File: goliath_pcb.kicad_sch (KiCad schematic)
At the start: 34 parts, among them IC1 MCT9001SD, IC2 MCT9001SD, IC3 MCT9001SD, IC4 MCT9001SD, IC5 MCT9001SD, IC6 LTC1298CS8-PBF, J1 RJ45_LED, J2 RJ45_LED, U1 Pico, U2 LM7805_TO220

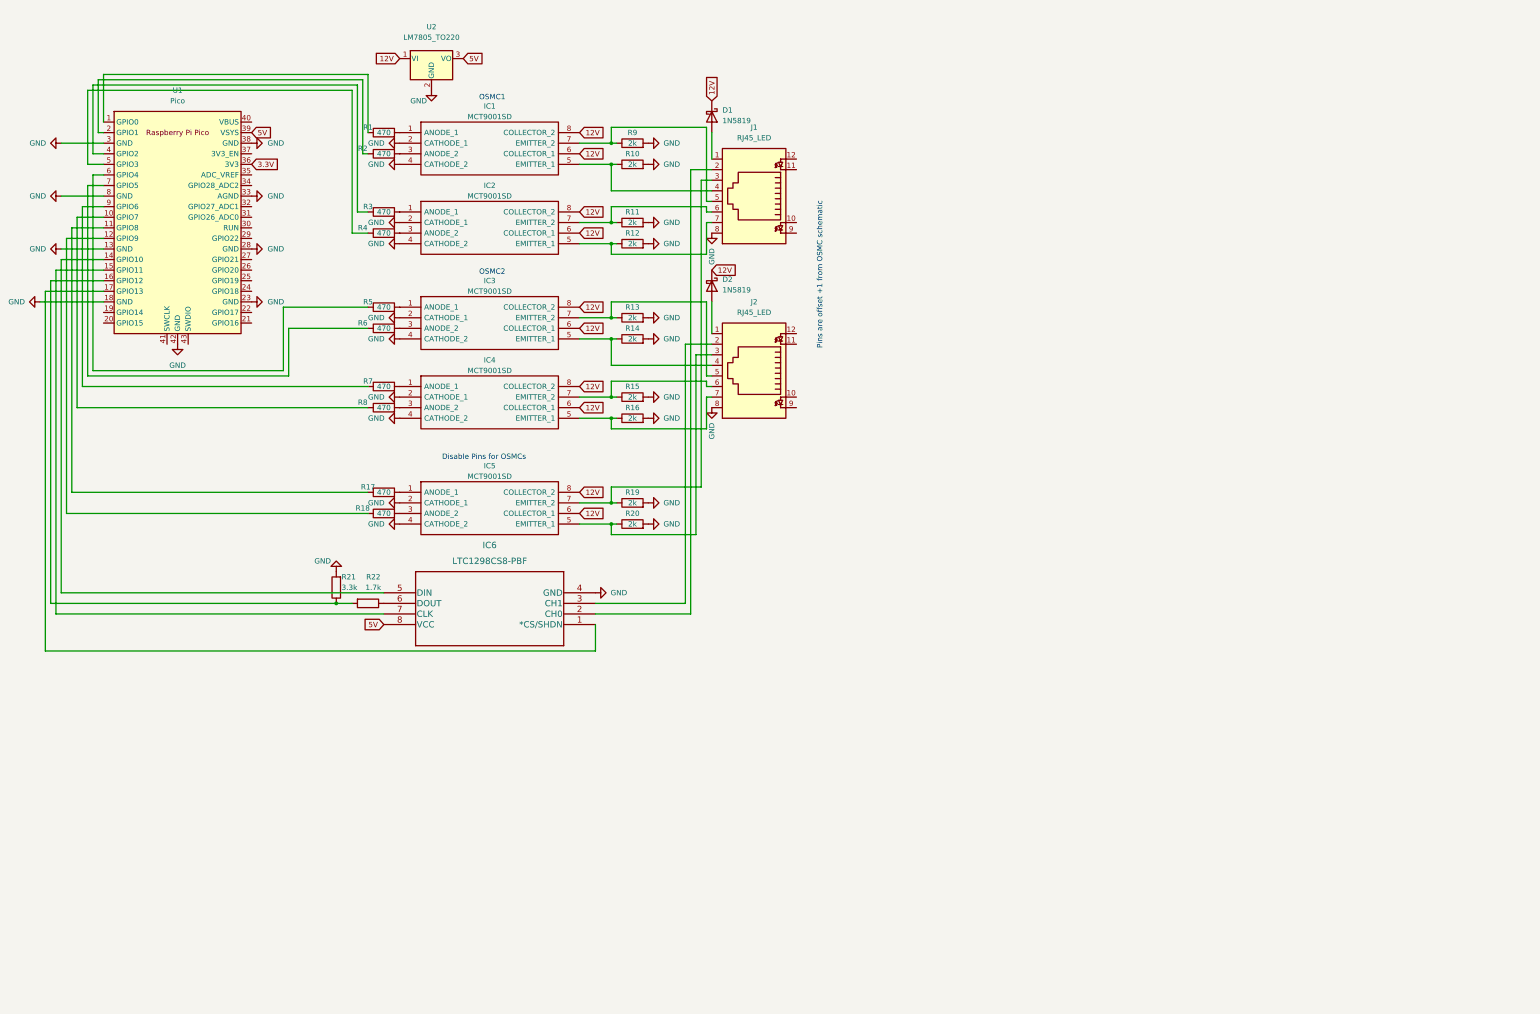
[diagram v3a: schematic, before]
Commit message: Add buffers, restart PCB layout, start encoder stuff
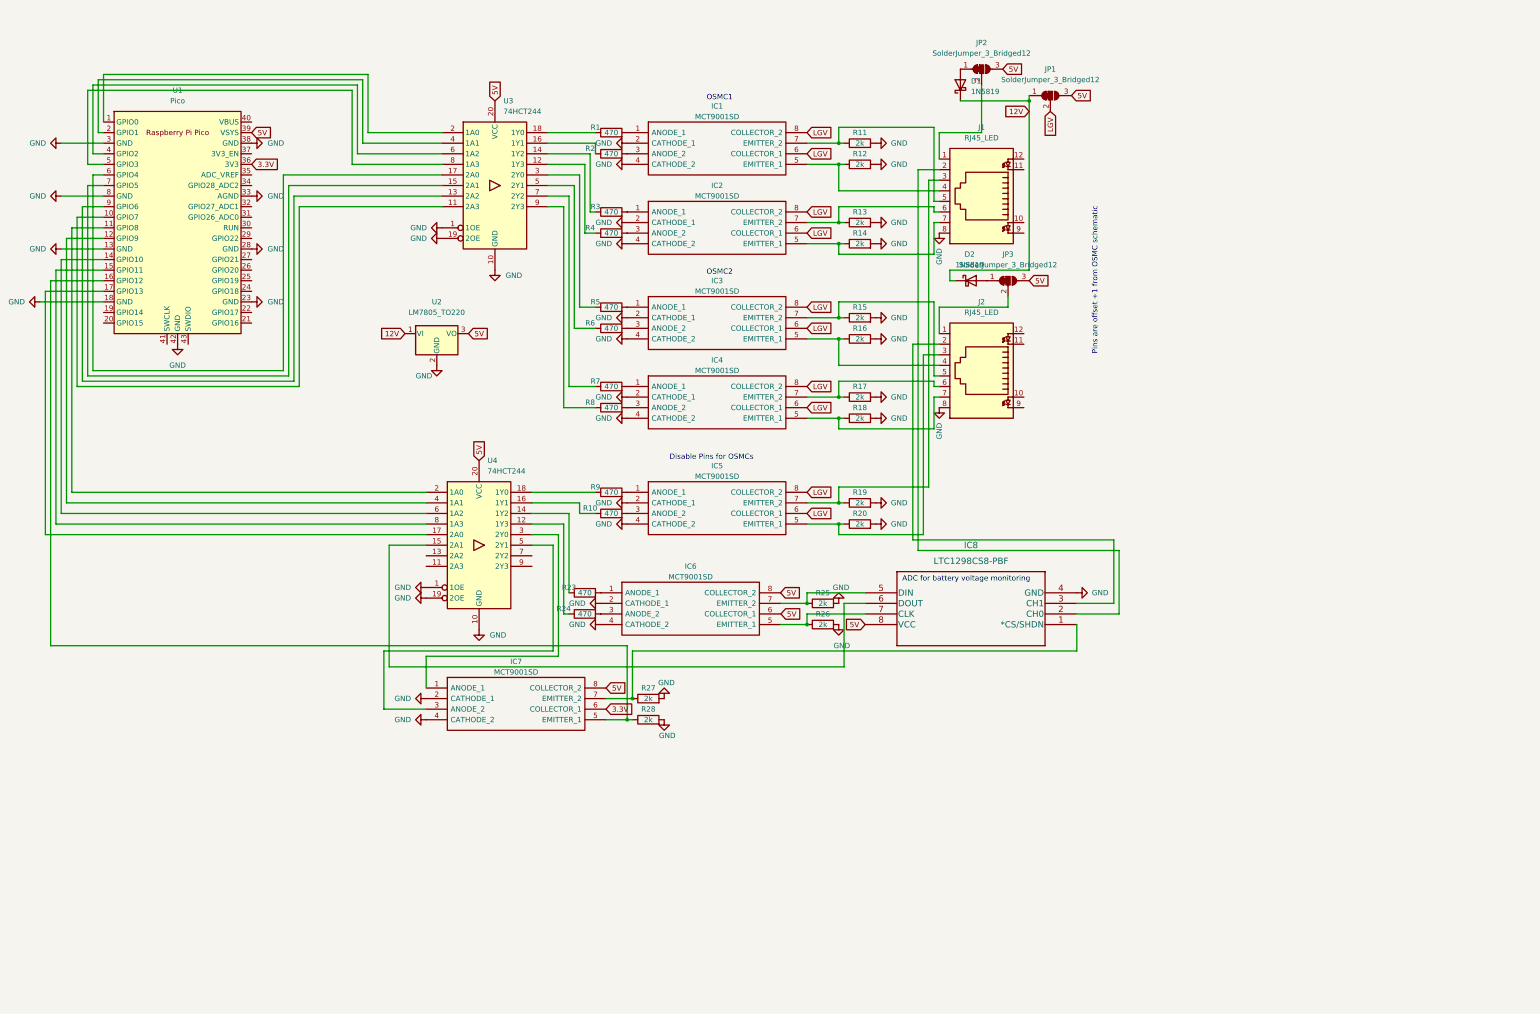
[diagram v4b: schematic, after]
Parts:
- removed R21: 3.3k, Resistor_THT:R_Axial_DIN0207_L6.3mm_D2.5mm_P10.16mm_Horizontal, symbol Device:R
- removed R22: 1.7k, Resistor_THT:R_Axial_DIN0207_L6.3mm_D2.5mm_P10.16mm_Horizontal, symbol Device:R
- added IC6, IC7: MCT9001SD, Package_DIP:DIP-8_W7.62mm_Socket, symbol MCT9001SD:MCT9001SD
- added JP1, JP2, JP3: SolderJumper_3_Bridged12, Jumper:SolderJumper-3_P1.3mm_Open_Pad1.0x1.5mm, symbol Jumper:SolderJumper_3_Bridged12
- added R23, R24: 470, Resistor_THT:R_Axial_DIN0207_L6.3mm_D2.5mm_P10.16mm_Horizontal, symbol Device:R
- added R25, R26, R27, R28: 2k, Resistor_THT:R_Axial_DIN0207_L6.3mm_D2.5mm_P10.16mm_Horizontal, symbol Device:R
- added U3, U4: 74HCT244, 74HCT241:CD74HCT241E, symbol 74xx:74HCT244
- IC1, IC2, IC3, IC4, IC5: footprint MCT9001:SOP254P1016X385-8N -> Package_DIP:DIP-8_W7.62mm_Socket
- IC8: renamed from IC6; footprint footprints:LTC1298CS8-PBF -> LTC1298:LTC1298CS8-PBF
- renumbered R18 to R10, R9 to R11, R10 to R12, R11 to R13, R12 to R14, R13 to R15, R14 to R16, R15 to R17, R16 to R18, R17 to R9
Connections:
- net 12V: now also JP1.1 (A); no longer IC1.6 (COLLECTOR_1), IC1.8 (COLLECTOR_2), IC2.6 (COLLECTOR_1), IC2.8 (COLLECTOR_2), IC3.6 (COLLECTOR_1), IC3.8 (COLLECTOR_2), IC4.6 (COLLECTOR_1), IC4.8 (COLLECTOR_2), IC5.6 (COLLECTOR_1), IC5.8 (COLLECTOR_2)
- net 3.3V: now also IC7.6 (COLLECTOR_1)
- net 5V: now also IC6.8 (COLLECTOR_2), IC7.8 (COLLECTOR_2), JP1.3 (B), JP2.3 (B), JP3.3 (B), U3.20 (VCC), U4.20 (VCC)
- net GND: now also IC6.2 (CATHODE_1), IC6.4 (CATHODE_2), IC7.2 (CATHODE_1), IC7.4 (CATHODE_2), R25.2, R26.2, R27.2, R28.2, U3.1 (1OE), U3.10 (GND), U3.19 (2OE), U4.1 (1OE), U4.10 (GND), U4.19 (2OE)
- net at R1.1: now also U3.18 (1Y0); no longer U1.1 (GPIO0)
- net at R7.1: now also U3.7 (2Y2); no longer U1.9 (GPIO6)
- net at IC8.1 (*CS/SHDN): now also IC7.7 (EMITTER_2), R27.1; no longer U1.17 (GPIO13)
- net at IC8.5 (DIN): now also IC6.7 (EMITTER_2), R25.1; no longer U1.14 (GPIO10)
- net at IC8.6 (DOUT): now also U4.15 (2A1)
- net at IC8.7 (CLK): now also IC6.5 (EMITTER_1), R26.1; no longer U1.15 (GPIO11)
- net at D2.2 (A): now also JP3.1 (A); no longer J2.1
- net at J1.1: now also JP2.2 (C); no longer D1.2 (A)
- net at R10.1: now also U4.16 (1Y1); no longer U1.12 (GPIO9)
- net at U1.16 (GPIO12): now also IC7.5 (EMITTER_1), R28.1
- net at R9.1: now also U4.18 (1Y0); no longer U1.11 (GPIO8)
- net at R3.1: now also U3.14 (1Y2); no longer U1.4 (GPIO2)
- net at U1.10 (GPIO7): now also U3.11 (2A3); no longer R8.1
- net at U1.7 (GPIO5): now also U3.15 (2A1); no longer R6.1
- net at R2.1: now also U3.16 (1Y1); no longer U1.2 (GPIO1)
- net at R4.1: now also U3.12 (1Y3); no longer U1.5 (GPIO3)
- net at U1.6 (GPIO4): now also U3.17 (2A0); no longer R5.1
- new net: IC6.1 (ANODE_1), R23.2
- new net: IC6.3 (ANODE_2), R24.2
- new net: J2.1, JP3.2 (C)
- new net: U1.9 (GPIO6), U3.13 (2A2)
- new net: U1.1 (GPIO0), U3.2 (1A0)
- new net: R5.1, U3.3 (2Y0)
- new net: U1.2 (GPIO1), U3.4 (1A1)
- new net: R6.1, U3.5 (2Y1)
- new net: U1.4 (GPIO2), U3.6 (1A2)
- new net: U1.5 (GPIO3), U3.8 (1A3)
- new net: R8.1, U3.9 (2Y3)
- new net: R24.1, U4.12 (1Y3)
- new net: R23.1, U4.14 (1Y2)
- new net: U1.17 (GPIO13), U4.17 (2A0)
- new net: U1.11 (GPIO8), U4.2 (1A0)
- new net: IC7.1 (ANODE_1), U4.3 (2Y0)
- new net: U1.12 (GPIO9), U4.4 (1A1)
- new net: IC7.3 (ANODE_2), U4.5 (2Y1)
- new net: U1.14 (GPIO10), U4.6 (1A2)
- new net: U1.15 (GPIO11), U4.8 (1A3)
- new net: D1.2 (A), JP2.1 (A)
- new net LGV: IC1.6 (COLLECTOR_1), IC1.8 (COLLECTOR_2), IC2.6 (COLLECTOR_1), IC2.8 (COLLECTOR_2), IC3.6 (COLLECTOR_1), IC3.8 (COLLECTOR_2), IC4.6 (COLLECTOR_1), IC4.8 (COLLECTOR_2), IC5.6 (COLLECTOR_1), IC5.8 (COLLECTOR_2), JP1.2 (C)
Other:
- note added: "ADC for battery voltage monitoring"
- moved on the sheet: D1, D2, IC1, IC2, IC3, IC4, IC5, IC8, J1, J2, R1, R10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

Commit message: Layout PCB
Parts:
- added J3, J4: RJ45_LED, Connector_RJ:RJ45_Amphenol_RJHSE538X, symbol Connector:RJ45_LED
- added JP4: SolderJumper_3_Bridged12, Jumper:SolderJumper-3_P1.3mm_Open_Pad1.0x1.5mm, symbol Jumper:SolderJumper_3_Bridged12
- added R25, R26: 470, Resistor_THT:R_Axial_DIN0207_L6.3mm_D2.5mm_P10.16mm_Horizontal, symbol Device:R
- added R29, R30, R31, R32, R33, R34: 10k, Resistor_THT:R_Axial_DIN0207_L6.3mm_D2.5mm_P10.16mm_Horizontal, symbol Device:R
- U3, U4: footprint 74HCT241:CD74HCT241E -> Package_DIP:DIP-20_W7.62mm_Socket
- U5: renamed from IC8; footprint LTC1298:LTC1298CS8-PBF -> Package_DIP:DIP-8_W7.62mm_Socket
- renumbered R23 to R21, R24 to R22, R25 to R23, R26 to R24
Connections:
- net 3.3V: now also JP4.3 (B), R29.1, R30.1, R31.1, R32.1, R33.1, R34.1
- net 5V: now also IC6.6 (COLLECTOR_1), J3.1, J3.2, J4.1, J4.2, JP4.1 (A); no longer JP1.3 (B)
- net GND: now also J3.6, J3.7, J3.8, J4.6, J4.7, J4.8
- net at U4.3 (2Y0): now also R25.2; no longer IC7.1 (ANODE_1)
- net at U4.5 (2Y1): now also R26.1; no longer IC7.3 (ANODE_2)
- net at U1.19 (GPIO14): now also J3.3, R31.2
- net at U1.20 (GPIO15): now also J3.4, R30.2
- net at U1.21 (GPIO16): now also J4.3, R34.2
- net at U1.22 (GPIO17): now also J4.4, R33.2
- new net: IC7.3 (ANODE_2), R26.2
- new net: J3.5, R29.2
- new net: J4.5, R32.2
- new net: JP1.3 (B), JP4.2 (C)
- new net: IC7.1 (ANODE_1), R25.1
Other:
- note added: "ADC Data"
- note added: "Black"
- note added: "Encoder connections"
- note added: "Orange"
- note added: "White"

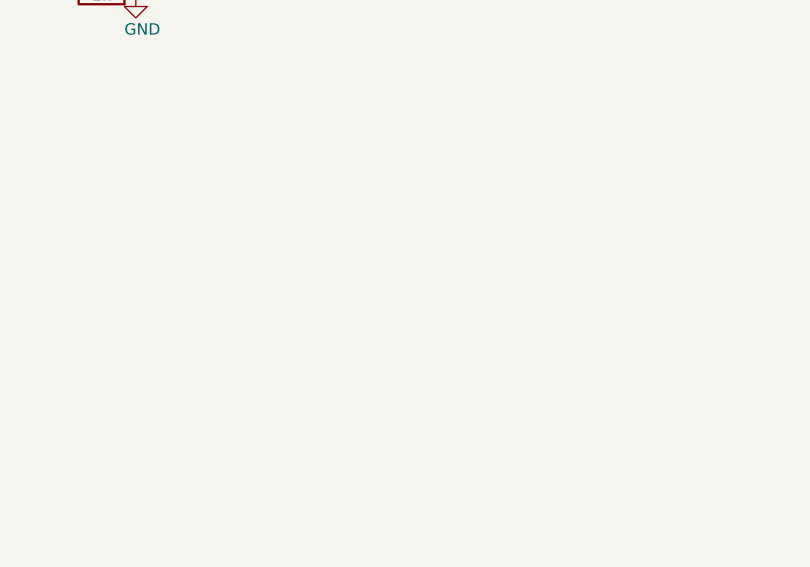
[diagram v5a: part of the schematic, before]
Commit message: Plan for xbee support
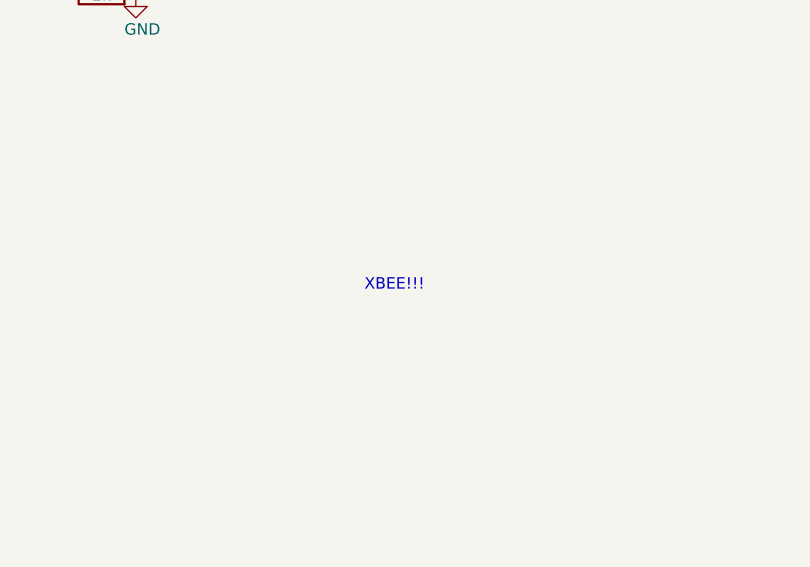
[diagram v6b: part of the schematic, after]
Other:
- note added: "XBEE!!!"
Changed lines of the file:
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@@
+    (effects (font (size 1.27 1.27)) (justify left bottom))
+  )
+  (text "XBEE!!!" (at 196.85 218.44 0)
     (effects (font (size 1.27 1.27)) (justify left bottom))
   )
